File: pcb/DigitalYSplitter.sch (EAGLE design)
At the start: 40 parts, among them CN1 Battery, CON1 USB_MICROSMT+THRUHULE, CON2 M05X2NO_SILK, CON3 LED_OUT, CON5 LED_OUT, Q1 16MHz, SW1 BUTTON_1, SW2 BUTTON_2, U1 MK20D--VFM5, U3 74LVC1G17DCK, U4 74LVC1G17DCK, U5 74LVC1G17DCK, U6 TPD4S012, U7 74LVC1G17DCK

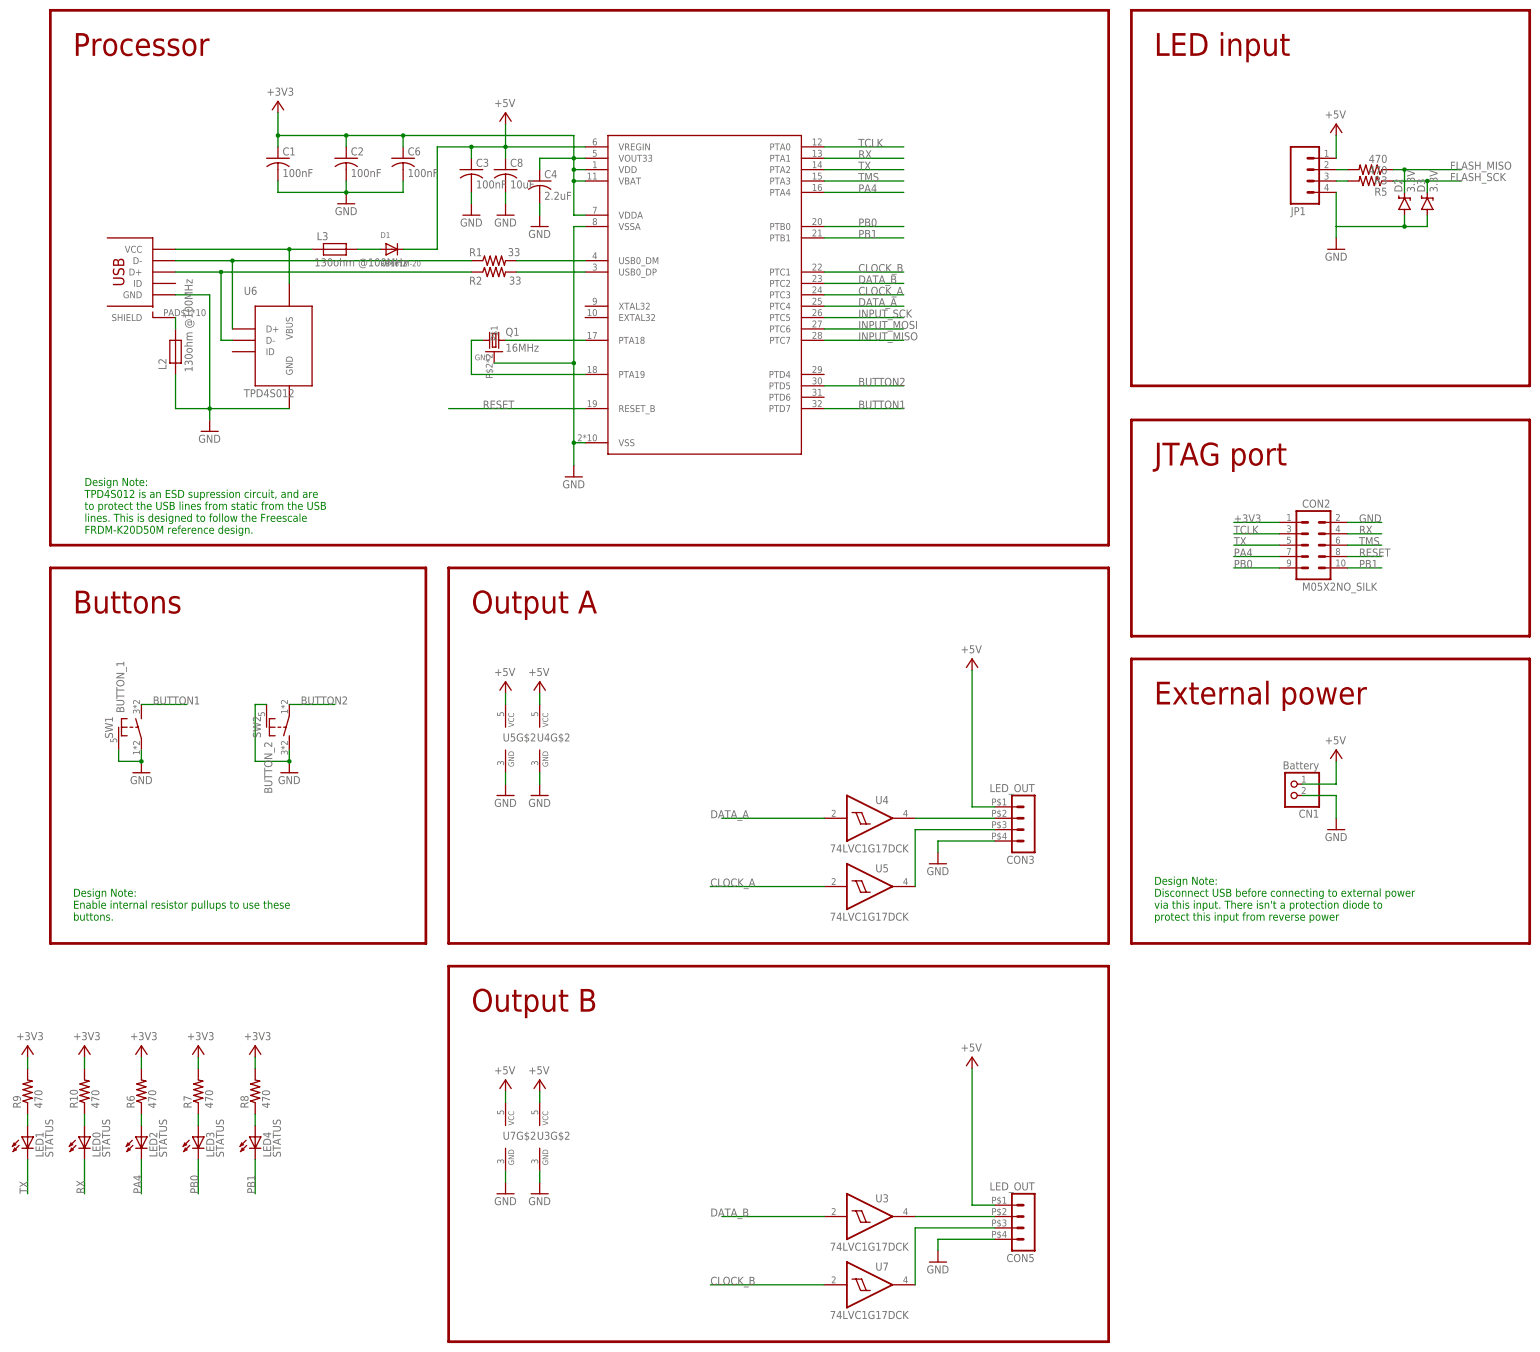
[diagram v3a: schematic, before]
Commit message: Workaround to test LED outputs, button inputs.
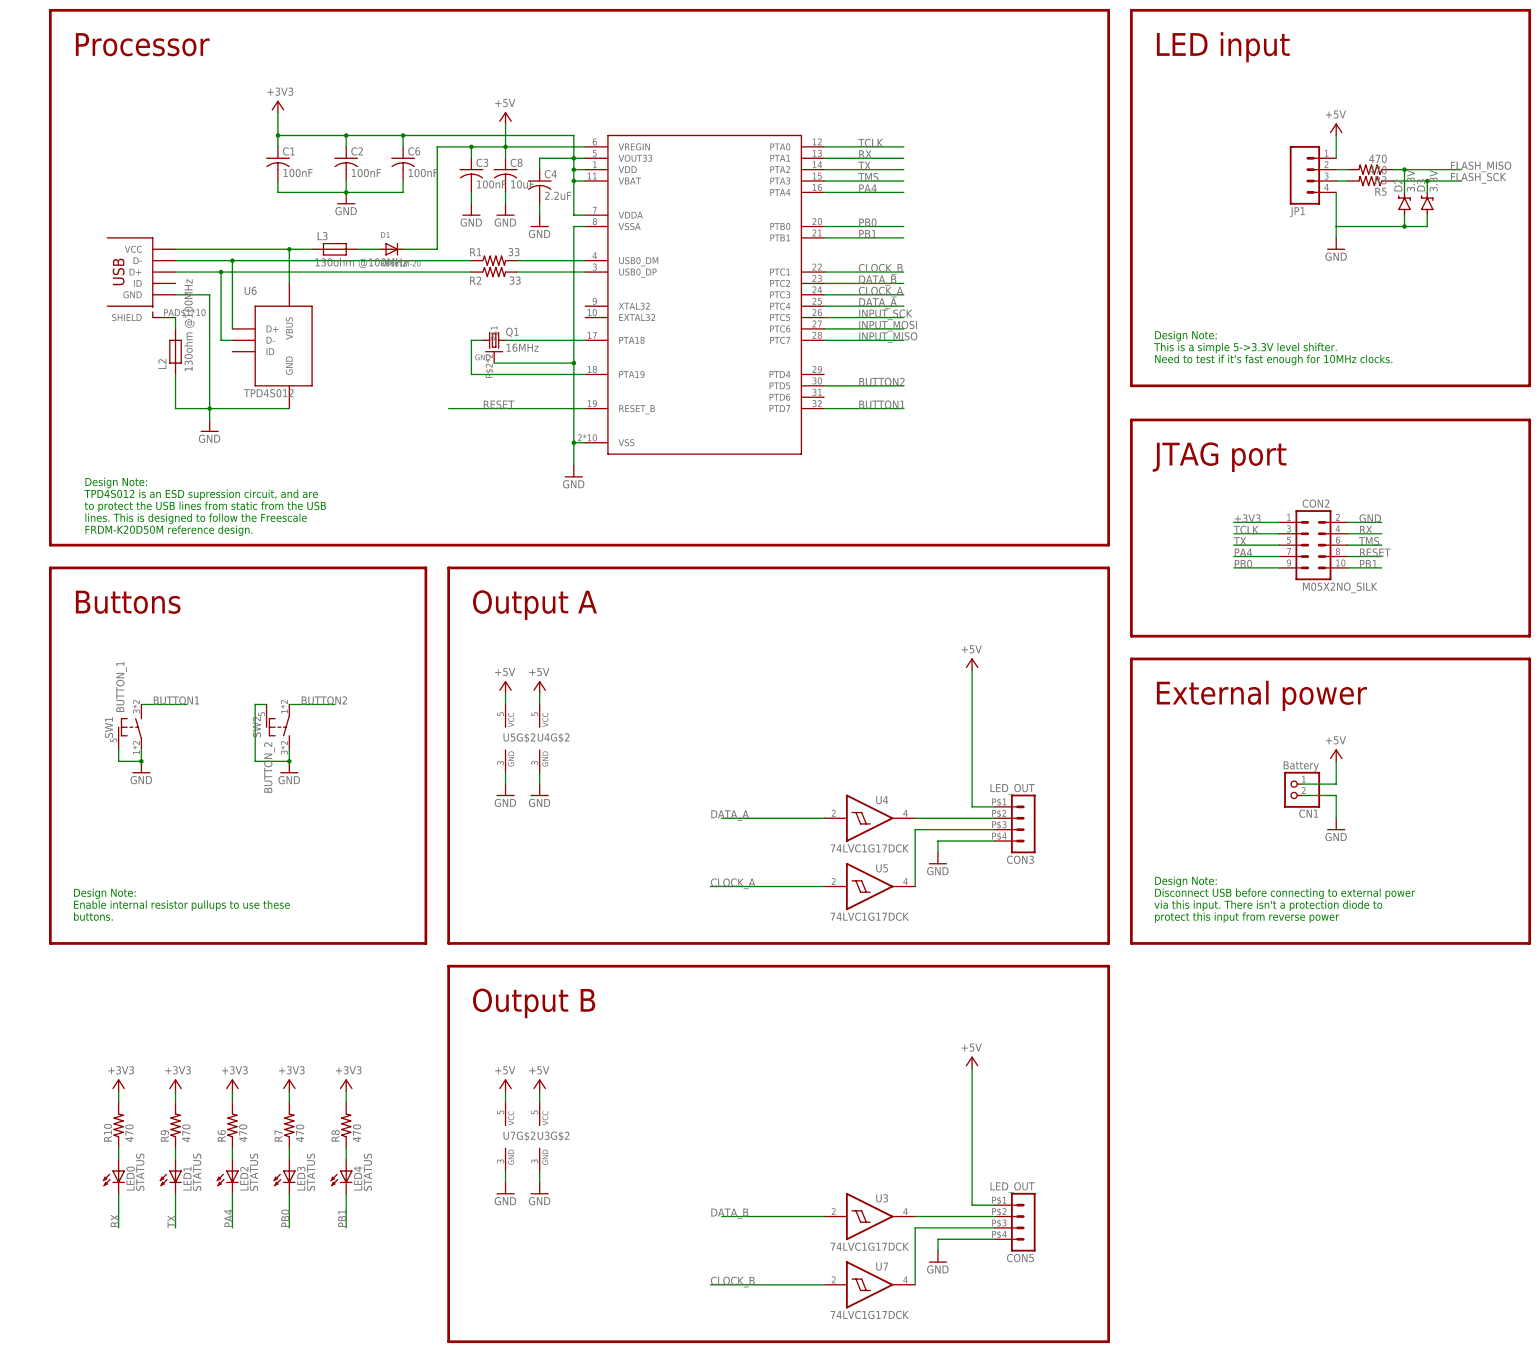
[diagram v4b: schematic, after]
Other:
- note added: "Design Note: This is a simple 5->3.3V level shifter. Need to test if it's fast enough for 10MHz clocks."
- moved on the sheet: LED0, LED1, LED2, LED3, LED4, R10, R6, R7, R8, R9
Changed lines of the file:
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@@
 <wire x1="251.46" y1="35.56" x2="251.46" y2="-48.26" width="0.6096" layer="94"/>
 <text x="109.22" y="25.4" size="5.08" layer="94">Output B</text>
+<text x="261.62" y="170.18" size="1.778" layer="91">Design Note:
+This is a simple 5-&gt;3.3V level shifter.
+Need to test if it's fast enough for 10MHz clocks.</text>
 </plain>
 <instances>
@@
 <instance part="D2" gate="G$1" x="317.5" y="205.74" rot="R90"/>
 <instance part="D3" gate="G$1" x="322.58" y="205.74" rot="R90"/>
-<instance part="R6" gate="G$1" x="35.56" y="7.62" rot="R90"/>
-<instance part="LED2" gate="G$1" x="35.56" y="-2.54"/>
-<instance part="3V1" gate="G$1" x="35.56" y="17.78" smashed="yes">
-<attribute name="VALUE" x="33.02" y="19.05" size="1.778" layer="96"/>
-</instance>
-<instance part="R7" gate="G$1" x="48.26" y="7.62" rot="R90"/>
-<instance part="LED3" gate="G$1" x="48.26" y="-2.54"/>
-<instance part="3V4" gate="G$1" x="48.26" y="17.78" smashed="yes">
-<attribute name="VALUE" x="45.72" y="19.05" size="1.778" layer="96"/>
-</instance>
-<instance part="R8" gate="G$1" x="60.96" y="7.62" rot="R90"/>
-<instance part="LED4" gate="G$1" x="60.96" y="-2.54"/>
-<instance part="3V5" gate="G$1" x="60.96" y="17.78" smashed="yes">
-<attribute name="VALUE" x="58.42" y="19.05" size="1.778" layer="96"/>
-</instance>
-<instance part="R9" gate="G$1" x="10.16" y="7.62" rot="R90"/>
-<instance part="LED1" gate="G$1" x="10.16" y="-2.54"/>
-<instance part="3V6" gate="G$1" x="10.16" y="17.78" smashed="yes">
-<attribute name="VALUE" x="7.62" y="19.05" size="1.778" layer="96"/>
-</instance>
-<instance part="R10" gate="G$1" x="22.86" y="7.62" rot="R90"/>
-<instance part="LED0" gate="G$1" x="22.86" y="-2.54"/>
-<instance part="3V7" gate="G$1" x="22.86" y="17.78" smashed="yes">
-<attribute name="VALUE" x="20.32" y="19.05" size="1.778" layer="96"/>
+<instance part="R6" gate="G$1" x="55.88" y="0" rot="R90"/>
+<instance part="LED2" gate="G$1" x="55.88" y="-10.16"/>
+<instance part="3V1" gate="G$1" x="55.88" y="10.16" smashed="yes">
+<attribute name="VALUE" x="53.34" y="11.43" size="1.778" layer="96"/>
+</instance>
+<instance part="R7" gate="G$1" x="68.58" y="0" rot="R90"/>
+<instance part="LED3" gate="G$1" x="68.58" y="-10.16"/>
+<instance part="3V4" gate="G$1" x="68.58" y="10.16" smashed="yes">
+<attribute name="VALUE" x="66.04" y="11.43" size="1.778" layer="96"/>
+</instance>
+<instance part="R8" gate="G$1" x="81.28" y="0" rot="R90"/>
+<instance part="LED4" gate="G$1" x="81.28" y="-10.16"/>
+<instance part="3V5" gate="G$1" x="81.28" y="10.16" smashed="yes">
+<attribute name="VALUE" x="78.74" y="11.43" size="1.778" layer="96"/>
+</instance>
+<instance part="R9" gate="G$1" x="43.18" y="0" rot="R90"/>
+<instance part="LED1" gate="G$1" x="43.18" y="-10.16"/>
+<instance part="3V6" gate="G$1" x="43.18" y="10.16" smashed="yes">
+<attribute name="VALUE" x="40.64" y="11.43" size="1.778" layer="96"/>
+</instance>
+<instance part="R10" gate="G$1" x="30.48" y="0" rot="R90"/>
+<instance part="LED0" gate="G$1" x="30.48" y="-10.16"/>
+<instance part="3V7" gate="G$1" x="30.48" y="10.16" smashed="yes">
+<attribute name="VALUE" x="27.94" y="11.43" size="1.778" layer="96"/>
 </instance>
 </instances>
@@
 <pinref part="3V1" gate="G$1" pin="+3V3"/>
 <pinref part="R6" gate="G$1" pin="2"/>
-<wire x1="35.56" y1="15.24" x2="35.56" y2="12.7" width="0.1524" layer="91"/>
+<wire x1="55.88" y1="7.62" x2="55.88" y2="5.08" width="0.1524" layer="91"/>
 </segment>
 <segment>
 <pinref part="3V4" gate="G$1" pin="+3V3"/>
 <pinref part="R7" gate="G$1" pin="2"/>
-<wire x1="48.26" y1="15.24" x2="48.26" y2="12.7" width="0.1524" layer="91"/>
+<wire x1="68.58" y1="7.62" x2="68.58" y2="5.08" width="0.1524" layer="91"/>
 </segment>
 <segment>
 <pinref part="3V5" gate="G$1" pin="+3V3"/>
 <pinref part="R8" gate="G$1" pin="2"/>
-<wire x1="60.96" y1="15.24" x2="60.96" y2="12.7" width="0.1524" layer="91"/>
+<wire x1="81.28" y1="7.62" x2="81.28" y2="5.08" width="0.1524" layer="91"/>
 </segment>
 <segment>
 <pinref part="3V6" gate="G$1" pin="+3V3"/>
 <pinref part="R9" gate="G$1" pin="2"/>
-<wire x1="10.16" y1="15.24" x2="10.16" y2="12.7" width="0.1524" layer="91"/>
+<wire x1="43.18" y1="7.62" x2="43.18" y2="5.08" width="0.1524" layer="91"/>
 </segment>
 <segment>
 <pinref part="3V7" gate="G$1" pin="+3V3"/>
 <pinref part="R10" gate="G$1" pin="2"/>
-<wire x1="22.86" y1="15.24" x2="22.86" y2="12.7" width="0.1524" layer="91"/>
+<wire x1="30.48" y1="7.62" x2="30.48" y2="5.08" width="0.1524" layer="91"/>
 </segment>
 </net>
@@
 <segment>
 <pinref part="LED0" gate="G$1" pin="C"/>
-<wire x1="22.86" y1="-7.62" x2="22.86" y2="-15.24" width="0.1524" layer="91"/>
-<label x="22.86" y="-15.24" size="1.778" layer="95" rot="R90"/>
+<wire x1="30.48" y1="-15.24" x2="30.48" y2="-22.86" width="0.1524" layer="91"/>
+<label x="30.48" y="-22.86" size="1.778" layer="95" rot="R90"/>
 </segment>
 </net>
@@
 <segment>
 <pinref part="LED1" gate="G$1" pin="C"/>
-<wire x1="10.16" y1="-7.62" x2="10.16" y2="-15.24" width="0.1524" layer="91"/>
-<label x="10.16" y="-15.24" size="1.778" layer="95" rot="R90"/>
+<wire x1="43.18" y1="-15.24" x2="43.18" y2="-22.86" width="0.1524" layer="91"/>
+<label x="43.18" y="-22.86" size="1.778" layer="95" rot="R90"/>
 </segment>
 </net>
@@
 <segment>
 <pinref part="LED2" gate="G$1" pin="C"/>
-<wire x1="35.56" y1="-7.62" x2="35.56" y2="-15.24" width="0.1524" layer="91"/>
-<label x="35.56" y="-15.24" size="1.778" layer="95" rot="R90"/>
+<wire x1="55.88" y1="-15.24" x2="55.88" y2="-22.86" width="0.1524" layer="91"/>
+<label x="55.88" y="-22.86" size="1.778" layer="95" rot="R90"/>
 </segment>
 </net>
@@
 <segment>
 <pinref part="LED3" gate="G$1" pin="C"/>
-<wire x1="48.26" y1="-7.62" x2="48.26" y2="-15.24" width="0.1524" layer="91"/>
-<label x="48.26" y="-15.24" size="1.778" layer="95" rot="R90"/>
+<wire x1="68.58" y1="-15.24" x2="68.58" y2="-22.86" width="0.1524" layer="91"/>
+<label x="68.58" y="-22.86" size="1.778" layer="95" rot="R90"/>
 </segment>
 </net>
@@
 <segment>
 <pinref part="LED4" gate="G$1" pin="C"/>
-<wire x1="60.96" y1="-7.62" x2="60.96" y2="-15.24" width="0.1524" layer="91"/>
-<label x="60.96" y="-15.24" size="1.778" layer="95" rot="R90"/>
+<wire x1="81.28" y1="-15.24" x2="81.28" y2="-22.86" width="0.1524" layer="91"/>
+<label x="81.28" y="-22.86" size="1.778" layer="95" rot="R90"/>
 </segment>
 </net>
@@
 <pinref part="R6" gate="G$1" pin="1"/>
 <pinref part="LED2" gate="G$1" pin="A"/>
-<wire x1="35.56" y1="2.54" x2="35.56" y2="0" width="0.1524" layer="91"/>
+<wire x1="55.88" y1="-5.08" x2="55.88" y2="-7.62" width="0.1524" layer="91"/>
 </segment>
 </net>
@@
 <pinref part="R7" gate="G$1" pin="1"/>
 <pinref part="LED3" gate="G$1" pin="A"/>
-<wire x1="48.26" y1="2.54" x2="48.26" y2="0" width="0.1524" layer="91"/>
+<wire x1="68.58" y1="-5.08" x2="68.58" y2="-7.62" width="0.1524" layer="91"/>
 </segment>
 </net>
@@
 <pinref part="R8" gate="G$1" pin="1"/>
 <pinref part="LED4" gate="G$1" pin="A"/>
-<wire x1="60.96" y1="2.54" x2="60.96" y2="0" width="0.1524" layer="91"/>
+<wire x1="81.28" y1="-5.08" x2="81.28" y2="-7.62" width="0.1524" layer="91"/>
 </segment>
 </net>
@@
 <pinref part="R9" gate="G$1" pin="1"/>
 <pinref part="LED1" gate="G$1" pin="A"/>
-<wire x1="10.16" y1="2.54" x2="10.16" y2="0" width="0.1524" layer="91"/>
+<wire x1="43.18" y1="-5.08" x2="43.18" y2="-7.62" width="0.1524" layer="91"/>
 </segment>
 </net>
@@
 <pinref part="R10" gate="G$1" pin="1"/>
 <pinref part="LED0" gate="G$1" pin="A"/>
-<wire x1="22.86" y1="2.54" x2="22.86" y2="0" width="0.1524" layer="91"/>
-</segment>
-</net>
+<wire x1="30.48" y1="-5.08" x2="30.48" y2="-7.62" width="0.1524" layer="91"/>
+</segment>
+</net>
